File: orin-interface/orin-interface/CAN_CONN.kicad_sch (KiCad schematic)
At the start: 1 part, among them J12 653105131822

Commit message: Finished: Orin-BoB
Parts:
- removed J12: 653105131822, Wurth_WR-WTB:J_Wurth_WR-WTB_653105131822, symbol Wurth_WR-WTB:653105131822
- added J6: 653104131822, Wurth_WR-WTB:J_Wurth_WR-WTB_653104131822, symbol Wurth_WR-WTB:653104131822
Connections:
- net CANH: now also J6.3
- net CANL: now also J6.2
- net GND: now also J6.4
- new net PWM: J6.1

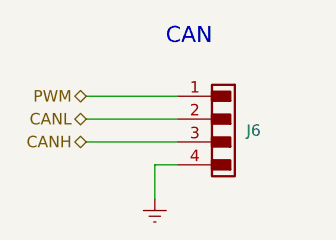
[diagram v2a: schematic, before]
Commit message: orin-interface: add ETH connector sheets and Mate-connectors footprint lib; update orin-bob
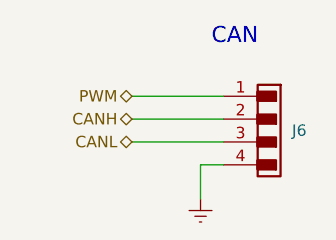
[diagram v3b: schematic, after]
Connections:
- net CANH: now also J6.2; no longer J6.3
- net CANL: now also J6.3; no longer J6.2
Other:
- moved on the sheet: J6
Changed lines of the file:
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@@
 	(text "CAN\n"
 		(exclude_from_sim no)
-		(at 105.41 50.546 0)
+		(at 110.49 50.546 0)
 		(effects
 			(font
@@
 	(wire
 		(pts
-			(xy 101.6 64.77) (xy 101.6 68.58)
-		)
-		(stroke
-			(width 0)
-			(type default)
-		)
-	)
-	(wire
-		(pts
-			(xy 93.98 59.69) (xy 104.14 59.69)
-		)
-		(stroke
-			(width 0)
-			(type default)
-		)
-	)
-	(wire
-		(pts
-			(xy 93.98 57.15) (xy 104.14 57.15)
-		)
-		(stroke
-			(width 0)
-			(type default)
-		)
-	)
-	(wire
-		(pts
-			(xy 104.14 64.77) (xy 101.6 64.77)
-		)
-		(stroke
-			(width 0)
-			(type default)
-		)
-	)
-	(wire
-		(pts
-			(xy 93.98 62.23) (xy 104.14 62.23)
+			(xy 106.68 64.77) (xy 106.68 68.58)
+		)
+		(stroke
+			(width 0)
+			(type default)
+		)
+	)
+	(wire
+		(pts
+			(xy 99.06 57.15) (xy 109.22 57.15)
+		)
+		(stroke
+			(width 0)
+			(type default)
+		)
+	)
+	(wire
+		(pts
+			(xy 109.22 64.77) (xy 106.68 64.77)
+		)
+		(stroke
+			(width 0)
+			(type default)
+		)
+	)
+	(wire
+		(pts
+			(xy 99.06 62.23) (xy 109.22 62.23)
+		)
+		(stroke
+			(width 0)
+			(type default)
+		)
+	)
+	(wire
+		(pts
+			(xy 99.06 59.69) (xy 109.22 59.69)
 		)
 		(stroke
@@
 	(hierarchical_label "CANL"
 		(shape bidirectional)
-		(at 93.98 59.69 180)
+		(at 99.06 62.23 180)
 		(effects
 			(font
@@
 	(hierarchical_label "PWM"
 		(shape bidirectional)
-		(at 93.98 57.15 180)
+		(at 99.06 57.15 180)
 		(effects
 			(font
@@
 	(hierarchical_label "CANH"
 		(shape bidirectional)
-		(at 93.98 62.23 180)
+		(at 99.06 59.69 180)
 		(effects
 			(font
@@
 	(symbol
 		(lib_id "Wurth_WR-WTB:653104131822")
-		(at 109.22 60.96 270)
+		(at 114.3 60.96 270)
 		(unit 1)
 		(body_style 1)
@@
 		(fields_autoplaced yes)
 		(property "Reference" "J6"
-			(at 111.76 60.9599 90)
+			(at 116.84 60.9599 90)
 			(show_name no)
 			(do_not_autoplace no)
@@
 		)
 		(property "Value" "653104131822"
-			(at 96.52 60.96 0)
+			(at 101.6 60.96 0)
 			(hide yes)
 			(show_name no)
@@
 		)
 		(property "Footprint" "Wurth_WR-WTB:J_Wurth_WR-WTB_653104131822"
-			(at 116.84 60.96 0)
+			(at 121.92 60.96 0)
 			(hide yes)
 			(show_name no)
@@
 		)
 		(property "Datasheet" "https://www.we-online.com/en/components/products/datasheet/653104131822?ki"
+			(at 132.08 106.68 0)
+			(hide yes)
+			(show_name no)
+			(do_not_autoplace no)
+			(effects
+				(font
+					(size 1.27 1.27)
+				)
+			)
+		)
+		(property "Description" "1.25 mm SMT Male Horizontal Shrouded Header"
+			(at 114.3 60.96 0)
+			(hide yes)
+			(show_name no)
+			(do_not_autoplace no)
+			(effects
+				(font
+					(size 1.27 1.27)
+				)
+			)
+		)
+		(property "Manufacturer" "Wurth Elektronik"
+			(at 129.54 106.68 0)
+			(hide yes)
+			(show_name no)
+			(do_not_autoplace no)
+			(effects
+				(font
+					(size 1.27 1.27)
+				)
+			)
+		)
+		(property "Manufacturer URL" "https://www.we-online.com"
 			(at 127 106.68 0)
 			(hide yes)
@@
 			)
 		)
-		(property "Description" "1.25 mm SMT Male Horizontal Shrouded Header"
-			(at 109.22 60.96 0)
-			(hide yes)
-			(show_name no)
-			(do_not_autoplace no)
-			(effects
-				(font
-					(size 1.27 1.27)
-				)
-			)
-		)
-		(property "Manufacturer" "Wurth Elektronik"
+		(property "Series" "WR-WTB"
 			(at 124.46 106.68 0)
 			(hide yes)
@@
 			)
 		)
-		(property "Manufacturer URL" "https://www.we-online.com"
+		(property "Pins (pcs)" "4"
 			(at 121.92 106.68 0)
 			(hide yes)
@@
 			)
 		)
-		(property "Series" "WR-WTB"
+		(property "Pitch (mm)" "1.25"
 			(at 119.38 106.68 0)
 			(hide yes)
@@
 			)
 		)
-		(property "Pins (pcs)" "4"
+		(property "Gender" "Male"
 			(at 116.84 106.68 0)
 			(hide yes)
@@
 			)
 		)
-		(property "Pitch (mm)" "1.25"
+		(property "Type" "Horizontal"
 			(at 114.3 106.68 0)
 			(hide yes)
@@
 			)
 		)
-		(property "Gender" "Male"
+		(property "Mounting Technology" "SMT"
 			(at 111.76 106.68 0)
 			(hide yes)
@@
 			)
 		)
-		(property "Type" "Horizontal"
+		(property "IR (A)" "1"
 			(at 109.22 106.68 0)
 			(hide yes)
@@
 			)
 		)
-		(property "Mounting Technology" "SMT"
+		(property "Working Voltage (V (AC))" "125"
 			(at 106.68 106.68 0)
 			(hide yes)
@@
 			)
 		)
-		(property "IR (A)" "1"
+		(property "PCB/Cable/Panel" "PCB"
 			(at 104.14 106.68 0)
 			(hide yes)
@@
 			)
 		)
-		(property "Working Voltage (V (AC))" "125"
+		(property "Contact Resistance (mohm)" "20"
 			(at 101.6 106.68 0)
 			(hide yes)
@@
 			)
 		)
-		(property "PCB/Cable/Panel" "PCB"
+		(property "Tol. R" "max."
 			(at 99.06 106.68 0)
 			(hide yes)
@@
 			)
 		)
-		(property "Contact Resistance (mohm)" "20"
+		(property "L (mm)" "9.75"
 			(at 96.52 106.68 0)
-			(hide yes)
-			(show_name no)
-			(do_not_autoplace no)
-			(effects
-				(font
-					(size 1.27 1.27)
-				)
-			)
-		)
-		(property "Tol. R" "max."
-			(at 93.98 106.68 0)
-			(hide yes)
-			(show_name no)
-			(do_not_autoplace no)
-			(effects
-				(font
-					(size 1.27 1.27)
-				)
-			)
-		)
-		(property "L (mm)" "9.75"
-			(at 91.44 106.68 0)
 			(hide yes)
 			(show_name no)
@@
 	(symbol
 		(lib_id "power:GNDREF")
-		(at 101.6 68.58 0)
+		(at 106.68 68.58 0)
 		(unit 1)
 		(body_style 1)
@@
 		(dnp no)
 		(property "Reference" "#PWR041"
-			(at 101.6 74.93 0)
+			(at 106.68 74.93 0)
 			(hide yes)
 			(show_name no)
@@
 		)
 		(property "Value" "GND"
-			(at 100.33 72.644 0)
+			(at 105.41 72.644 0)
 			(hide yes)
 			(show_name no)
@@
 		)
 		(property "Footprint" ""
-			(at 101.6 68.58 0)
+			(at 106.68 68.58 0)
 			(hide yes)
 			(show_name no)
@@
 		)
 		(property "Datasheet" ""
-			(at 101.6 68.58 0)
+			(at 106.68 68.58 0)
 			(hide yes)
 			(show_name no)
@@
 		)
 		(property "Description" "Power symbol creates a global label with name \"GNDREF\" , reference supply ground"
-			(at 101.6 68.58 0)
-			(hide yes)
-			(show_name no)
+			(at 106.68 68.58 0)
+			(hide yes)
+			(show_name no)
